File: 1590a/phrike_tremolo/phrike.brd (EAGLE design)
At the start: 33 x 41.9 mm, 37 parts, among them Q1 2N5457, Q2 2N3904, Q3 2N5457, Q4 2N5088

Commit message: finished chorus and tremolo baords; other tweaks & polish
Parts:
- moved D1 1.91 mm to (13.3, 34.9)
- moved R13 1.90 mm to (14.6, 27.9)
- moved 9V 0.90 mm to (18.4, 38.7)
- moved R10 0.64 mm to (6.35, 32.4)
- moved R11 0.64 mm to (6.35, 34.9)
- moved C5 0.64 mm to (30.5, 17.1)
- moved C6 0.64 mm to (5.08, 29.8)
- moved Q3 0.64 mm to (5.08, 26.0)
- moved R6 0.64 mm to (19.7, 6.35)
- moved D2 0.64 mm to (19.7, 3.17)
- moved GND 0.64 mm to (24.1, 3.17)
- moved IN 0.64 mm to (15.2, 3.17)
- moved OUT 0.64 mm to (27.3, 3.17)
- moved VOLUME 0.63 mm to (29.2, 8.89)
- moved C1 0.63 mm to (18.4, 33.7)
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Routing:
- net N$11: track 2.80 -> 10.3 mm
- net N$17: track 0.00 -> 4.86 mm
- net N$7: track 24.4 -> 28.2 mm
- net N$14: track 16.6 -> 13.2 mm
- net N$15: track 13.6 -> 11.2 mm
- net N$13: track 43.0 -> 45.0 mm
- net IN: track 17.5 -> 15.6 mm
- net N$16: track 11.4 -> 9.83 mm
- net N$3: track 28.5 -> 27.2 mm
- net +9V: track 2.84 -> 3.81 mm
- net N$1: track 25.4 -> 24.6 mm
- net N$4: track 20.4 -> 19.6 mm
- net N$9: track 6.24 -> 5.61 mm
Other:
- board size 33 x 41.9 mm -> 33 x 41.3 mm
- board text added: "(c)2016"
- board text added: "PHRIKE"
- board text added: "TREMOLO"
- board text added: "by burr settles"

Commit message: added RT logo; converted some pots trimmers
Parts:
- added U$2: (no value), logos:RT150
- DEPTH: device potentiometers:PADS_SMALL -> potentiometers:2262_TRIM
- moved C6 1.90 mm to (5.08, 27.9)
- moved R10 1.90 mm to (6.35, 30.5)
- moved R11 1.90 mm to (6.35, 33.0)
- moved Q3 1.27 mm to (5.08, 24.8)
- moved D1 0.64 mm to (13.3, 35.6)
- moved R9 0.64 mm to (2.54, 18.4)
- moved C2 0.63 mm to (7.62, 6.99)
- moved IN 0.63 mm to (14.6, 3.17)
- moved Q1 0.63 mm to (11.4, 6.99)
- moved R1 0.63 mm to (2.54, 5.71)
- moved R3 0.63 mm to (5.08, 5.71)
- moved R4 0.63 mm to (6.35, 12.1)
- moved 9V 0.63 mm to (18.4, 39.4)
- moved C4 0.63 mm to (6.35, 19.1)
- moved D2 0.63 mm to (19.1, 3.17)
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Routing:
- net N$7: track 28.2 -> 32.3 mm
- net N$15: track 11.2 -> 13.2 mm
- net N$11: track 10.3 -> 12.2 mm
- net N$10: track 13.8 -> 11.8 mm
- net N$16: track 9.83 -> 11.6 mm
- net N$17: track 4.86 -> 6.13 mm
- net IN: track 15.6 -> 16.8 mm
- net N$9: track 5.61 -> 4.96 mm
- net N$8: track 9.72 -> 9.09 mm
- net N$13: track 45.0 -> 44.4 mm
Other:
- board size 33 x 41.3 mm -> 33 x 41.9 mm
- board text added: "burr settles"
- board text removed: "by burr settles"

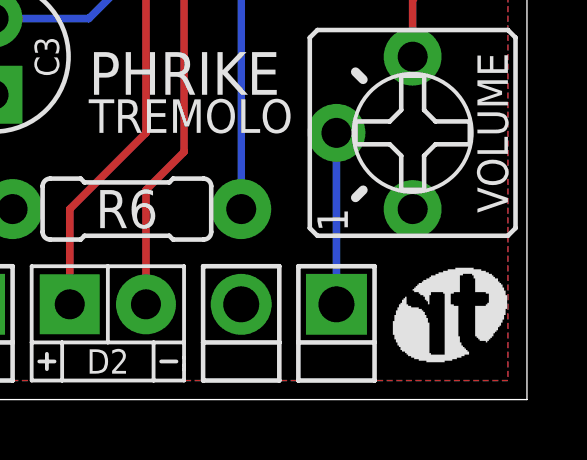
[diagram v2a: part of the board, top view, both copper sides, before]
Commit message: convert bitmap logos to polygons
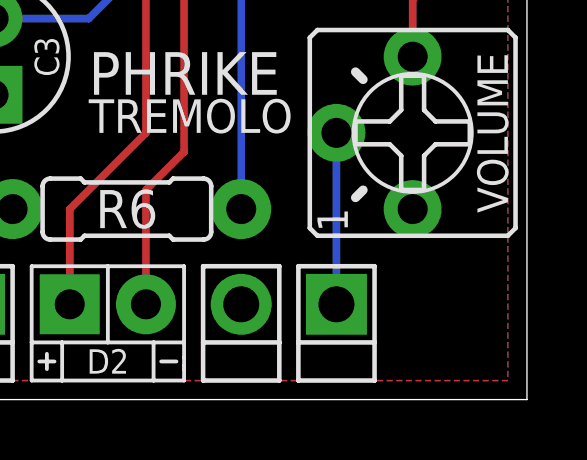
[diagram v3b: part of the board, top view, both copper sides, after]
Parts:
- U$2: device logos:RT150 -> logos:RT0150
- moved U$2 2.29 mm to (30.5, 2.54)
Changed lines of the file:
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@@
 <element name="C1" library="capacitors-elec" package="063_025" value="100u" x="18.415" y="33.655"/>
 <element name="9V" library="jacks" package="DC" value="DC_MONO" x="18.415" y="39.37" rot="MR0"/>
-<element name="U$2" library="logos" package="RT150" value="" x="28.575" y="1.27"/>
+<element name="U$2" library="logos" package="RT0150" value="" x="30.48" y="2.54"/>
 </elements>
 <signals>
